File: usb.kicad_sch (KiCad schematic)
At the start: 36 parts, among them J10 Screw_Terminal_01x02, J2 Screw_Terminal_01x03, J4 Conn_ARM_SWD_TagConnect_TC2030, J5 Conn_01x06_Pin, J6 Conn_01x06_Pin, J7 Conn_01x06_Pin, J8 Screw_Terminal_01x02, J9 Screw_Terminal_01x02, Q10 L8050QLT1G, Q3 LMBT3906DW1T1G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

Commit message: parts assigned, footprints checked
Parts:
- J2: LCSC (none) -> C5632696
- R10: LCSC (none) -> C22809
- R15, R21: LCSC (none) -> C22548
- R16: LCSC (none) -> C122970
- R17: LCSC (none) -> C14675
- R18, R19, R20, R9: LCSC (none) -> C116677
- R22, R27: LCSC (none) -> C110637
- R28, R29: LCSC (none) -> C25819
- U3, U4: LCSC (none) -> C3009245
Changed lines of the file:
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@@
 		(property "LCSC" "C77055"
 			(at 252.73 91.4399 0)
+			(hide yes)
+			(show_name no)
+			(do_not_autoplace no)
 			(effects
 				(font
 					(size 1.27 1.27)
 				)
-				(hide yes)
 			)
 		)
@@
 			)
 		)
+		(property "LCSC" "C122970"
+			(at 87.63 62.23 0)
+			(hide yes)
+			(show_name no)
+			(do_not_autoplace no)
+			(effects
+				(font
+					(size 1.27 1.27)
+				)
+			)
+		)
 		(pin "1"
 		)
@@
 			)
 		)
+		(property "LCSC" "C22548"
+			(at 60.96 121.92 0)
+			(hide yes)
+			(show_name no)
+			(do_not_autoplace no)
+			(effects
+				(font
+					(size 1.27 1.27)
+				)
+			)
+		)
 		(pin "1"
 		)
@@
 		(property "LCSC" "C5632695"
 			(at 185.42 33.02 0)
+			(hide yes)
+			(show_name no)
+			(do_not_autoplace no)
 			(effects
 				(font
 					(size 1.27 1.27)
 				)
-				(hide yes)
 			)
 		)
@@
 		(property "LCSC" "C77055"
 			(at 252.73 43.1799 0)
+			(hide yes)
+			(show_name no)
+			(do_not_autoplace no)
 			(effects
 				(font
 					(size 1.27 1.27)
 				)
-				(hide yes)
 			)
 		)
@@
 			)
 		)
+		(property "LCSC" "C110637"
+			(at 205.74 29.21 0)
+			(hide yes)
+			(show_name no)
+			(do_not_autoplace no)
+			(effects
+				(font
+					(size 1.27 1.27)
+				)
+			)
+		)
 		(pin "2"
 		)
@@
 			)
 		)
+		(property "LCSC" "C116677"
+			(at 46.99 121.92 0)
+			(hide yes)
+			(show_name no)
+			(do_not_autoplace no)
+			(effects
+				(font
+					(size 1.27 1.27)
+				)
+			)
+		)
 		(pin "2"
 		)
@@
 			)
 		)
+		(property "LCSC" "C116677"
+			(at 124.968 54.864 0)
+			(hide yes)
+			(show_name no)
+			(do_not_autoplace no)
+			(effects
+				(font
+					(size 1.27 1.27)
+				)
+			)
+		)
 		(pin "1"
 		)
@@
 			)
 		)
+		(property "LCSC" "C3009245"
+			(at 227.33 78.74 0)
+			(hide yes)
+			(show_name no)
+			(do_not_autoplace no)
+			(effects
+				(font
+					(size 1.27 1.27)
+				)
+			)
+		)
 		(pin "4"
 		)
@@
 			)
 		)
+		(property "LCSC" "C5632696"
+			(at 27.94 119.38 0)
+			(hide yes)
+			(show_name no)
+			(do_not_autoplace no)
+			(effects
+				(font
+					(size 1.27 1.27)
+				)
+			)
+		)
 		(pin "1"
 		)
@@
 			)
 		)
+		(property "LCSC" "C116677"
+			(at 124.968 52.832 0)
+			(hide yes)
+			(show_name no)
+			(do_not_autoplace no)
+			(effects
+				(font
+					(size 1.27 1.27)
+				)
+			)
+		)
 		(pin "1"
 		)
@@
 			)
 		)
+		(property "LCSC" "C116677"
+			(at 124.968 56.896 0)
+			(hide yes)
+			(show_name no)
+			(do_not_autoplace no)
+			(effects
+				(font
+					(size 1.27 1.27)
+				)
+			)
+		)
 		(pin "1"
 		)
@@
 		(property "LCSC" "C49581"
 			(at 217.17 137.1599 0)
+			(hide yes)
+			(show_name no)
+			(do_not_autoplace no)
 			(effects
 				(font
 					(size 1.27 1.27)
 				)
-				(hide yes)
 			)
 		)
@@
 			)
 		)
+		(property "LCSC" "C25819"
+			(at 246.38 77.4699 0)
+			(hide yes)
+			(show_name no)
+			(do_not_autoplace no)
+			(effects
+				(font
+					(size 1.27 1.27)
+				)
+			)
+		)
 		(pin "2"
 		)
@@
 			)
 		)
+		(property "LCSC" "C14675"
+			(at 96.52 49.5301 0)
+			(hide yes)
+			(show_name no)
+			(do_not_autoplace no)
+			(effects
+				(font
+					(size 1.27 1.27)
+				)
+			)
+		)
 		(pin "1"
 		)
@@
 			)
 		)
+		(property "LCSC" "C110637"
+			(at 205.74 77.47 0)
+			(hide yes)
+			(show_name no)
+			(do_not_autoplace no)
+			(effects
+				(font
+					(size 1.27 1.27)
+				)
+			)
+		)
 		(pin "2"
 		)
@@
 		(property "LCSC" "C5632695"
 			(at 250.19 135.89 0)
+			(hide yes)
+			(show_name no)
+			(do_not_autoplace no)
 			(effects
 				(font
 					(size 1.27 1.27)
 				)
-				(hide yes)
 			)
 		)
@@
 			)
 		)
+		(property "LCSC" "C22548"
+			(at 199.39 132.08 0)
+			(hide yes)
+			(show_name no)
+			(do_not_autoplace no)
+			(effects
+				(font
+					(size 1.27 1.27)
+				)
+			)
+		)
 		(pin "2"
 		)
@@
 			)
 		)
+		(property "LCSC" "C22809"
+			(at 50.8 134.6199 0)
+			(hide yes)
+			(show_name no)
+			(do_not_autoplace no)
+			(effects
+				(font
+					(size 1.27 1.27)
+				)
+			)
+		)
 		(pin "2"
 		)
@@
 			)
 		)
+		(property "LCSC" "C3009245"
+			(at 227.33 30.48 0)
+			(hide yes)
+			(show_name no)
+			(do_not_autoplace no)
+			(effects
+				(font
+					(size 1.27 1.27)
+				)
+			)
+		)
 		(pin "4"
 		)
@@
 		(property "LCSC" "C5632695"
 			(at 185.42 81.28 0)
+			(hide yes)
+			(show_name no)
+			(do_not_autoplace no)
 			(effects
 				(font
 					(size 1.27 1.27)
 				)
-				(hide yes)
 			)
 		)
@@
 			)
 		)
+		(property "LCSC" "C25819"
+			(at 246.38 29.2099 0)
+			(hide yes)
+			(show_name no)
+			(do_not_autoplace no)
+			(effects
+				(font
+					(size 1.27 1.27)
+				)
+			)
+		)
 		(pin "2"
 		)
@@
 		(property "LCSC" "C77055"
 			(at 64.77 134.6199 0)
+			(hide yes)
+			(show_name no)
+			(do_not_autoplace no)
 			(effects
 				(font
 					(size 1.27 1.27)
 				)
-				(hide yes)
 			)
 		)

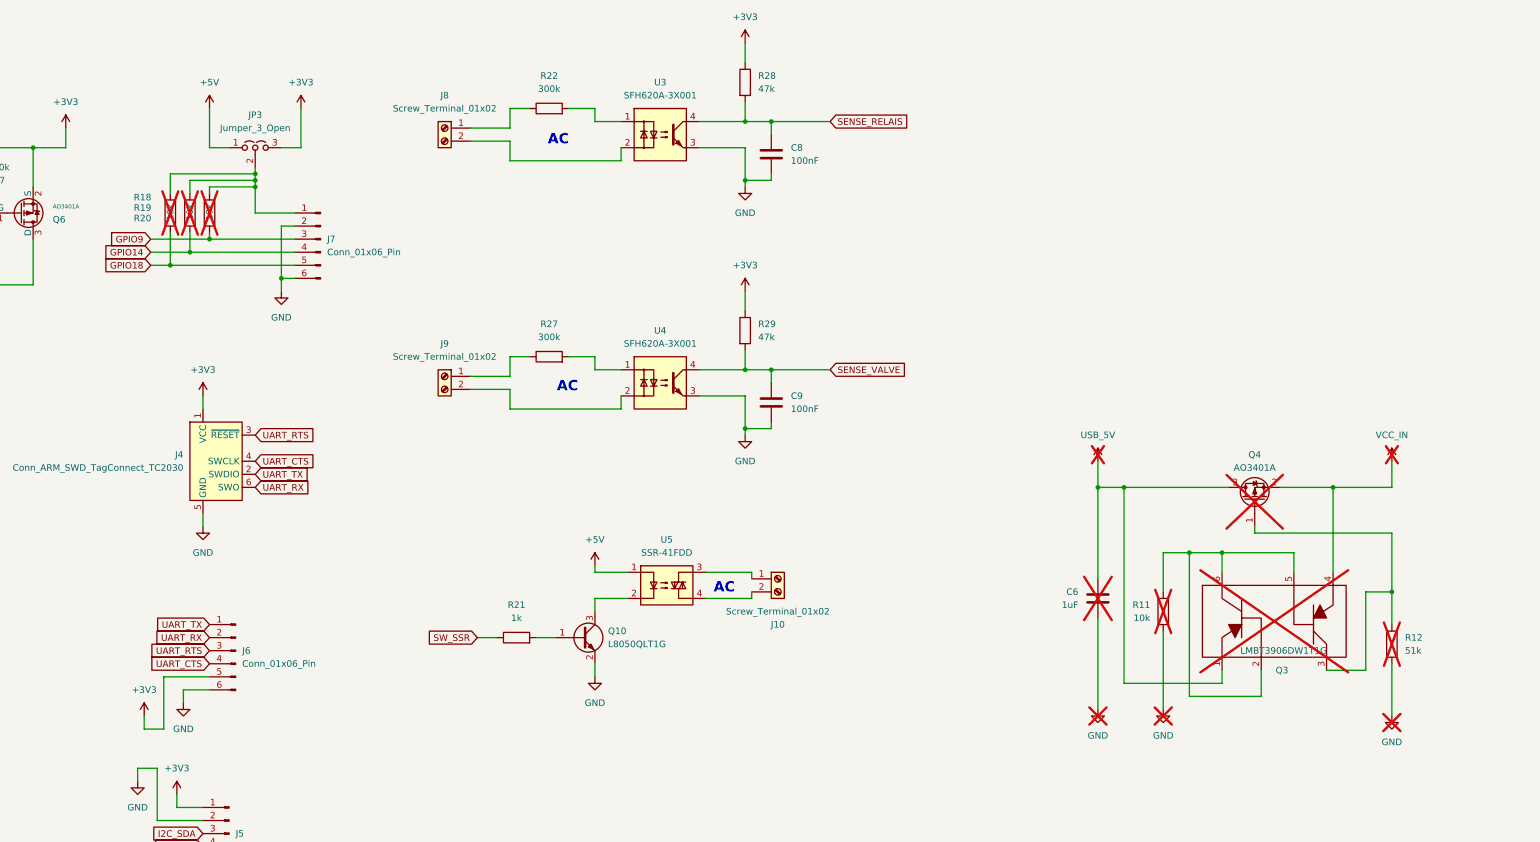
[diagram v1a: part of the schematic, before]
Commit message: started pcb layout
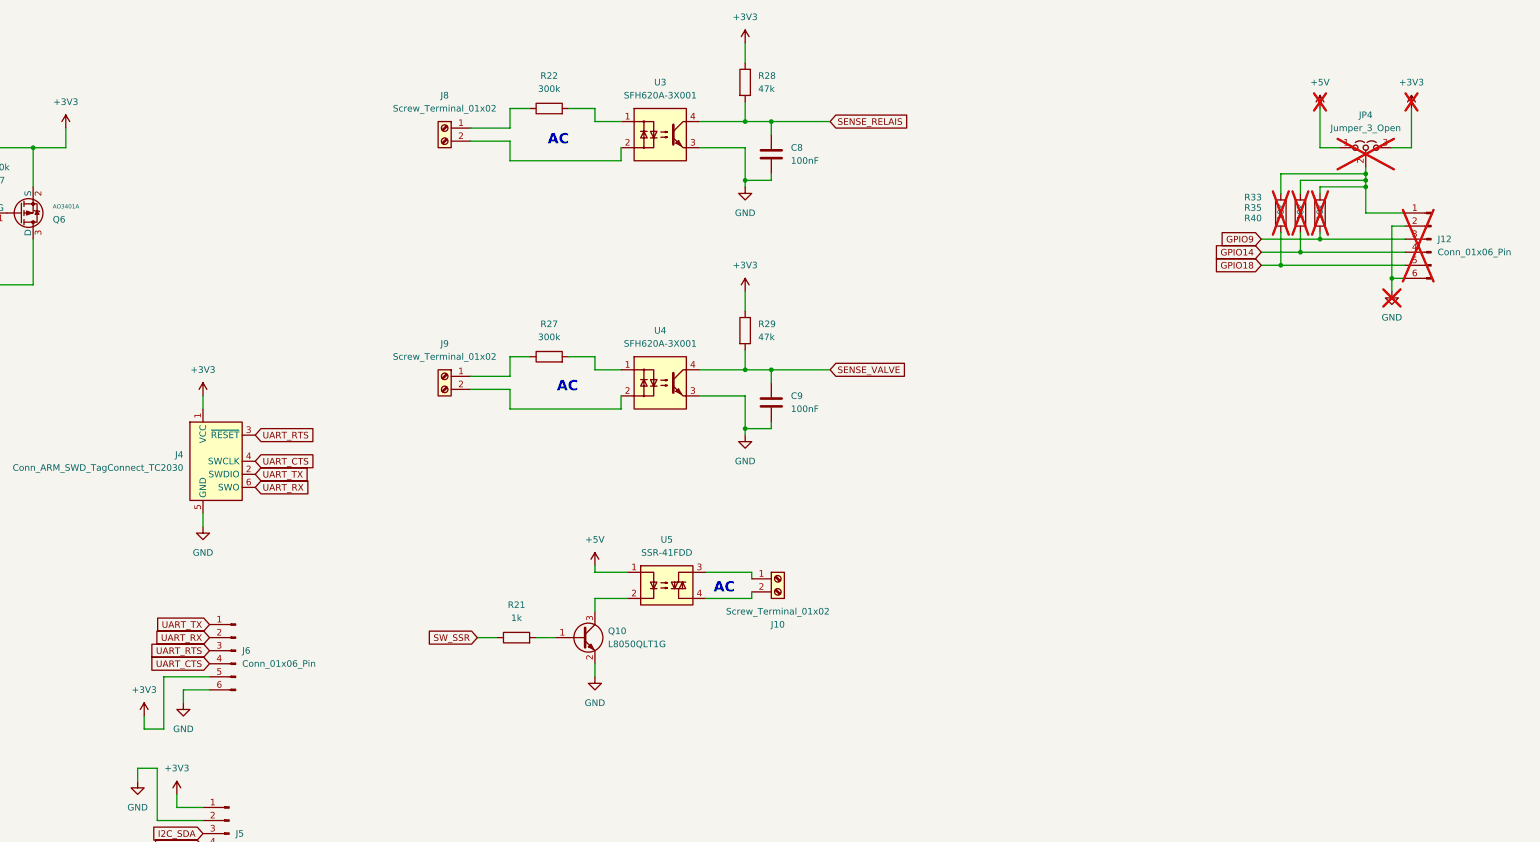
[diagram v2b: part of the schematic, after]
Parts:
- removed C6: 1uF, symbol Device:C
- removed J7: Conn_01x06_Pin, Connector_PinHeader_2.54mm:PinHeader_1x06_P2.54mm_Vertical, symbol Connector:Conn_01x06_Pin
- removed JP3: Jumper_3_Open, Connector:FanPinHeader_1x03_P2.54mm_Vertical, symbol Jumper:Jumper_3_Open
- removed Q3: LMBT3906DW1T1G, PCM_JLCPCB:SOT-363_SC-70-6, symbol markus:LMBT3906DW1T1G
- removed Q4: AO3401A, Package_TO_SOT_SMD:SOT-23, symbol Transistor_FET:AO3401A
- removed R11: 10k, symbol Device:R
- removed R12: 51k, symbol Device:R
- removed R18, R19, R20: 10k, PCM_JLCPCB:R_0603, symbol Device:R
- added J12: Conn_01x06_Pin, Connector_PinHeader_2.54mm:PinHeader_1x06_P2.54mm_Vertical, symbol Connector:Conn_01x06_Pin
- added JP4: Jumper_3_Open, Connector:FanPinHeader_1x03_P2.54mm_Vertical, symbol Jumper:Jumper_3_Open
- added R33, R35, R40: 10k, PCM_JLCPCB:R_0603, symbol Device:R
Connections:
- net +3V3: now also JP4.3 (B)
- net +5V: now also JP4.1 (A)
- net GND: now also J12.2 (Pin_2), J12.6 (Pin_6)
- net GPIO14: now also J12.4 (Pin_4), R35.2
- net GPIO18: now also J12.5 (Pin_5), R33.2
- net GPIO9: now also J12.3 (Pin_3), R40.2
- new net: J12.1 (Pin_1), JP4.2 (C), R33.1, R35.1, R40.1

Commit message: routing finished v0.1.0
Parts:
- added TP4, TP6: TestPoint, TestPoint:TestPoint_Pad_D1.5mm, symbol Connector:TestPoint
- added TP5, TP7: TestPoint, TestPoint:TestPoint_Pad_1.5x1.5mm, symbol Connector:TestPoint
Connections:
- net +5V: now also TP4.1, TP6.1
- net GND: now also TP5.1, TP7.1
